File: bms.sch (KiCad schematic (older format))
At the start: 19 parts, among them J1 Conn_01x02_Male, J2 Conn_01x02_Male, J3 Conn_01x02_Female, U1 BQ24160RGET

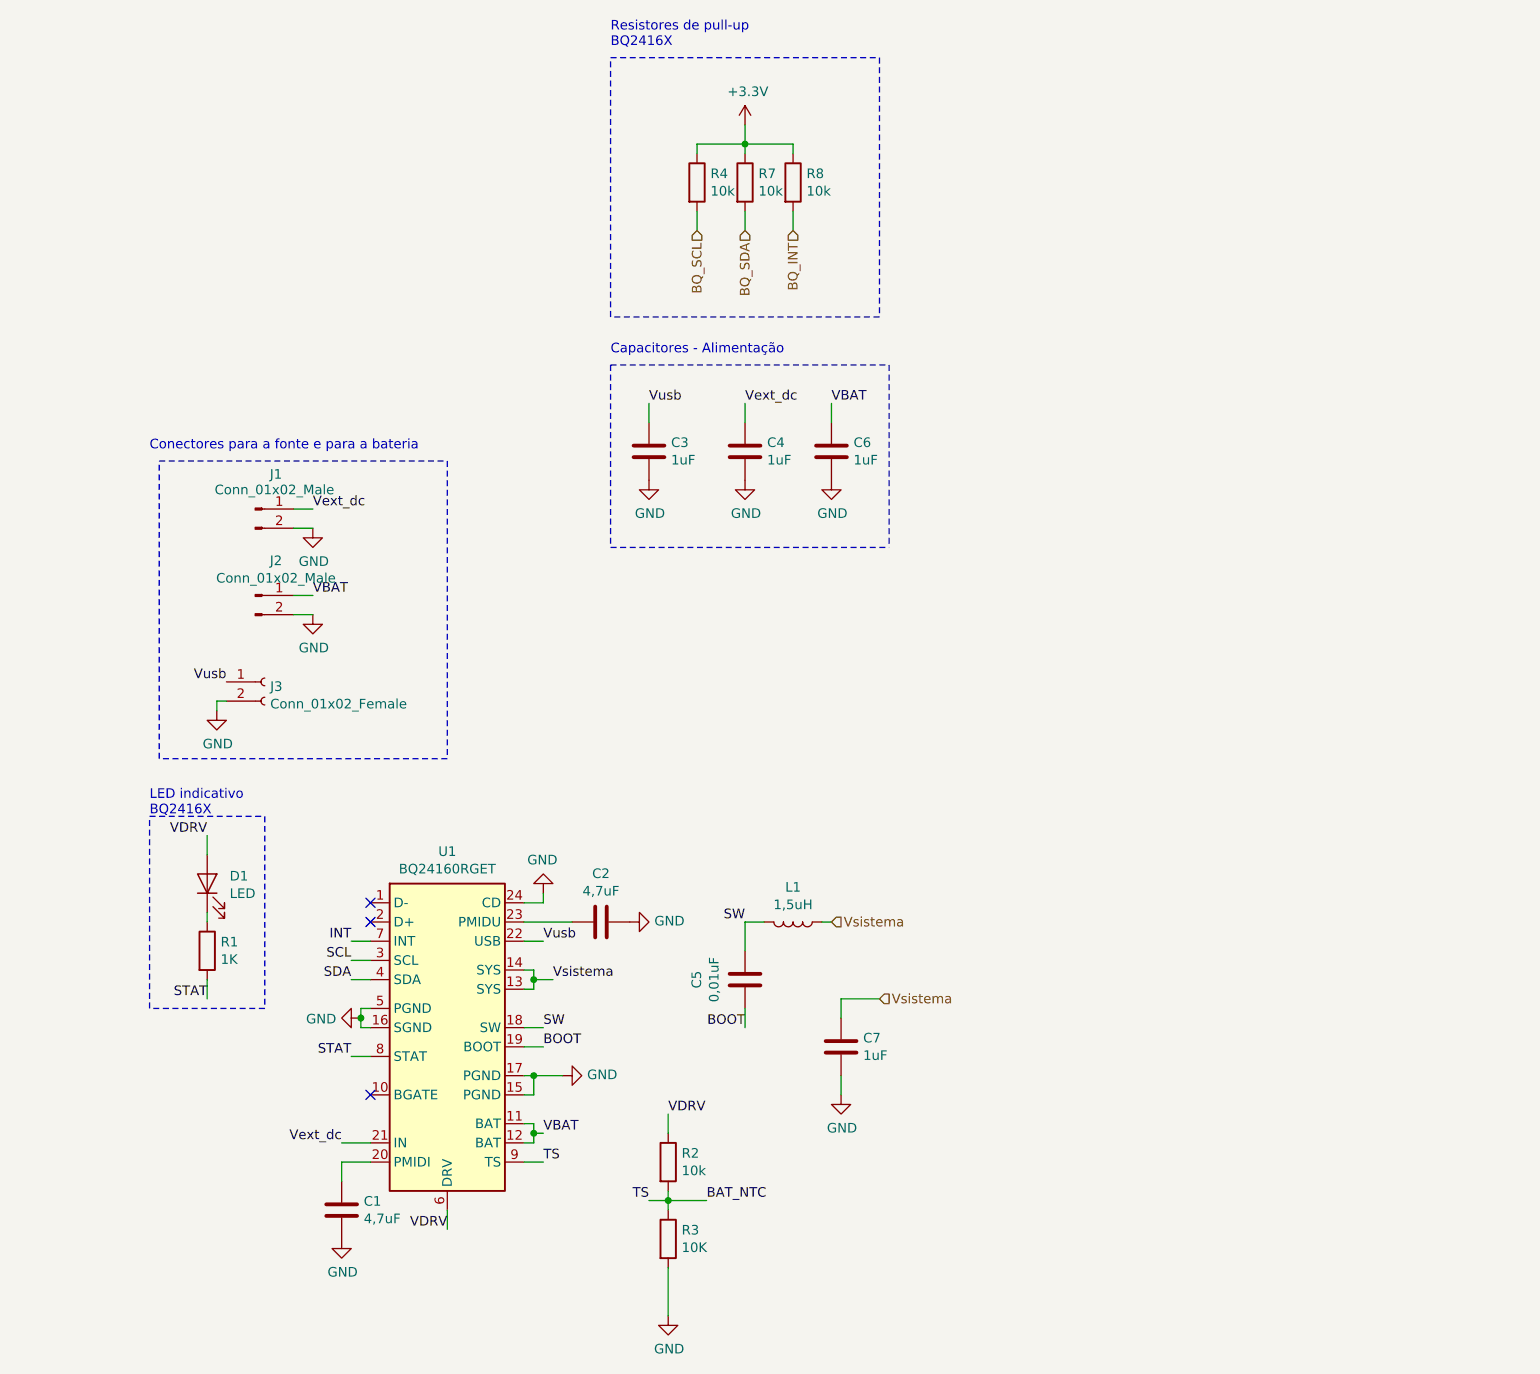
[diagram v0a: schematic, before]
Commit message: Adicionando radio LoRa. Criando um .sch para a Raspberry e para o radio
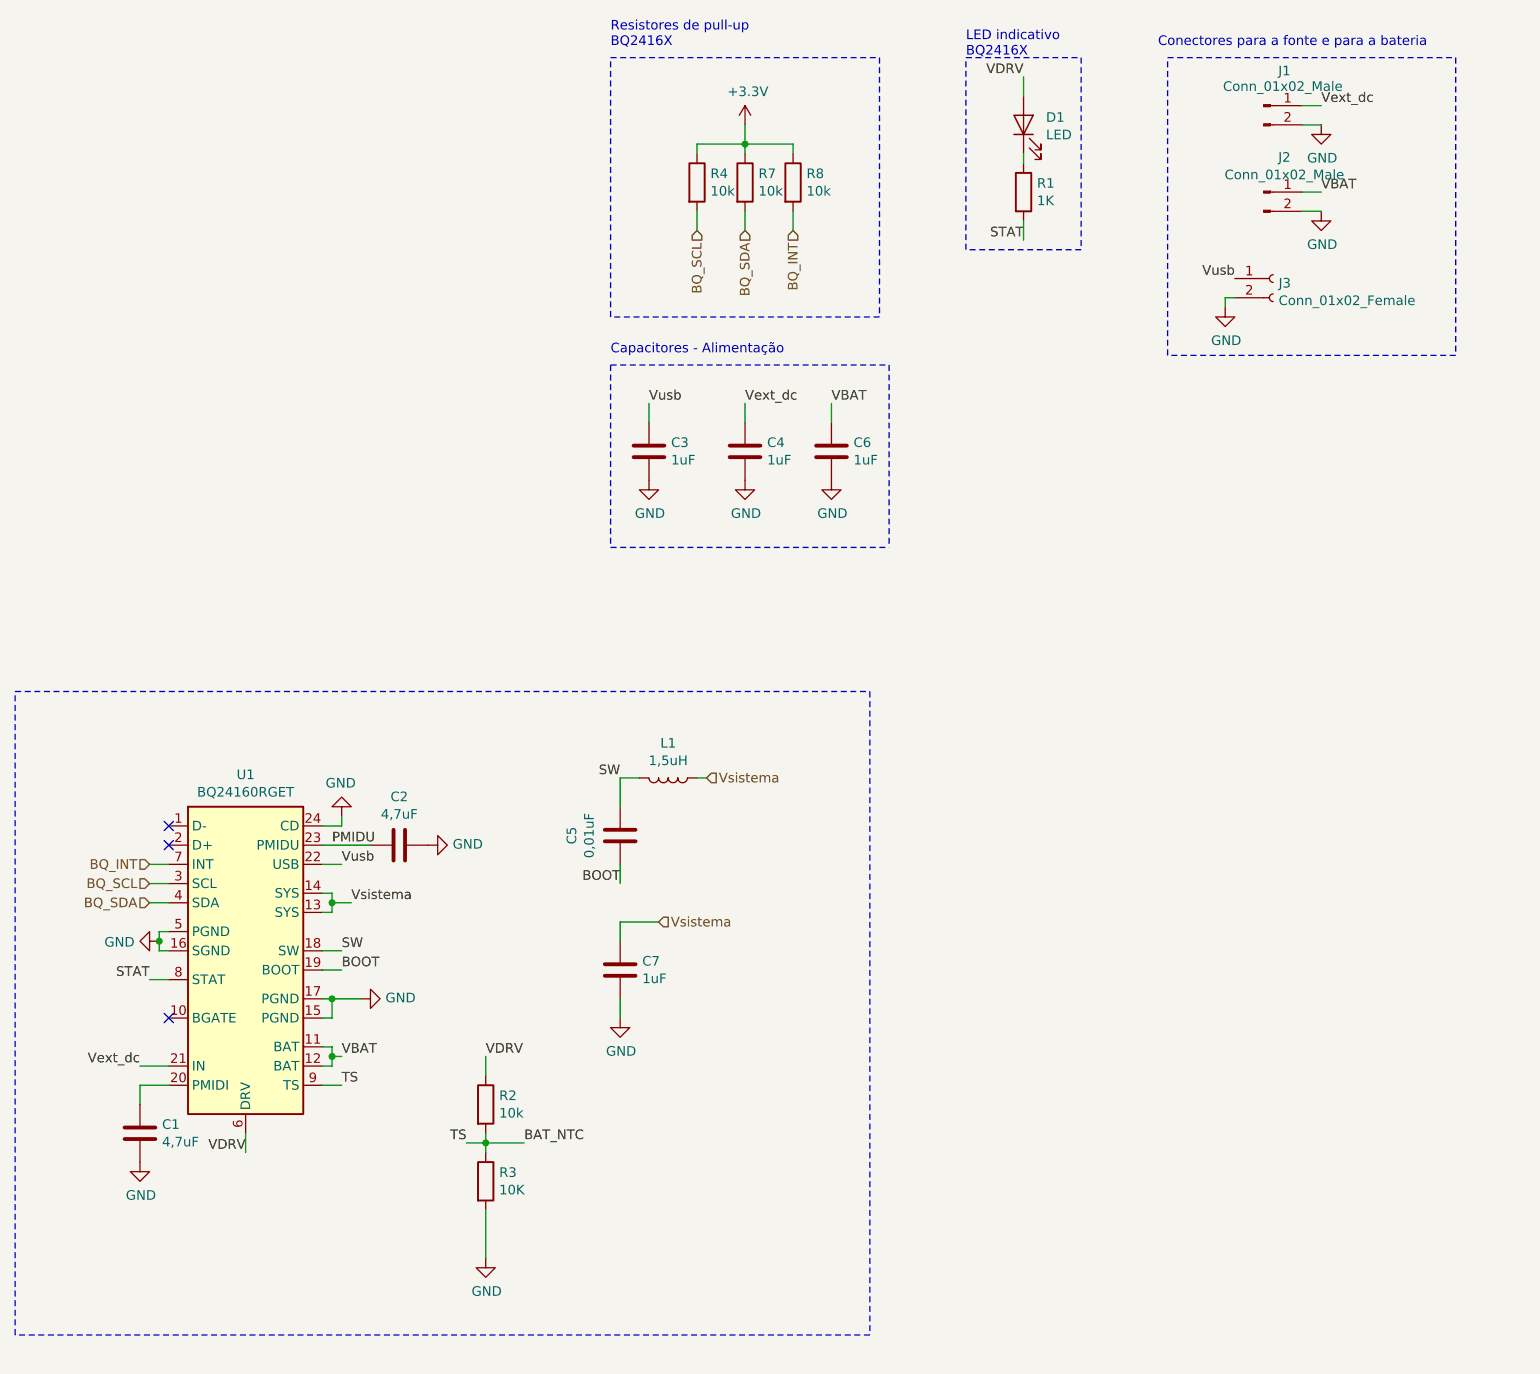
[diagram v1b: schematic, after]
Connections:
- net INT is gone; now on net BQ_INT: U1.7 (INT)
- net SCL is gone; now on net BQ_SCL: U1.3 (SCL)
- net SDA is gone; now on net BQ_SDA: U1.4 (SDA)
- net PMIDU: now reaches C2.2, U1.23 (PMIDU)
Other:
- moved on the sheet: C1, C2, C5, C7, D1, J1, J2, J3, L1, R1, R2, R3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
